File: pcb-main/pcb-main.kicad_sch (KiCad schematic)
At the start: 37 parts, among them J1 AVR-ISP-6, J2 Conn_02x06_Counter_Clockwise, M1 Stepper_Motor, SW1 SW_MEC_5E, SW2 SW_MEC_5E, U1 ATmega328P-AU, U2 HT1621B-LQFP-A, U3 VIM878, U4 PCF8563T, Y1 16MHz, Y2 32kHz

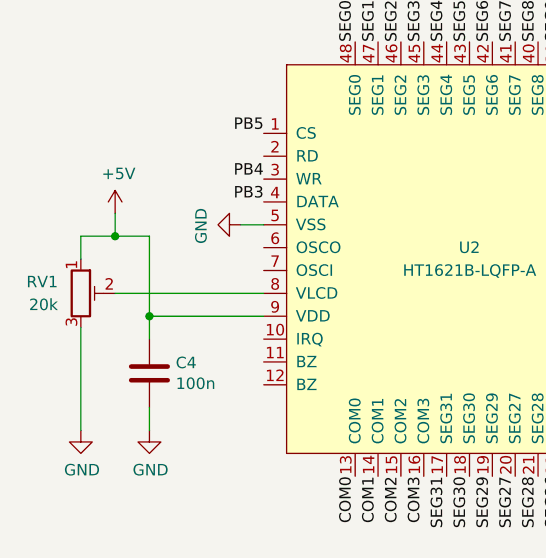
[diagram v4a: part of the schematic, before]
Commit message: changed pot
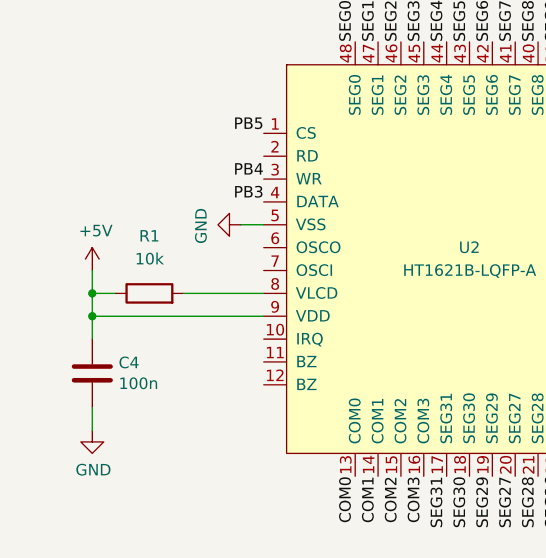
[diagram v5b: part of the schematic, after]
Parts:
- removed RV1: 20k, Potentiometer_SMD:Potentiometer_Bourns_TC33X_Vertical, symbol Device:R_Potentiometer_Trim
- added R1: 10k, Resistor_SMD:R_1206_3216Metric_Pad1.30x1.75mm_HandSolder, symbol Device:R
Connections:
- net +5V: now also R1.1
- net at U2.8 (VLCD): now also R1.2
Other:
- moved on the sheet: C4
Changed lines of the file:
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@@
   (junction (at 217.17 45.72) (diameter 0) (color 0 0 0 0)
   )
+  (junction (at 27.94 161.29) (diameter 0) (color 0 0 0 0)
+  )
   (junction (at 262.89 24.13) (diameter 0) (color 0 0 0 0)
   )
-  (junction (at 34.29 163.83) (diameter 0) (color 0 0 0 0)
-  )
   (junction (at 273.05 36.83) (diameter 0) (color 0 0 0 0)
   )
   (junction (at 227.33 63.5) (diameter 0) (color 0 0 0 0)
   )
-  (junction (at 30.48 154.94) (diameter 0) (color 0 0 0 0)
-  )
   (junction (at 186.69 36.83) (diameter 0) (color 0 0 0 0)
   )
@@
   (junction (at 227.33 50.8) (diameter 0) (color 0 0 0 0)
   )
+  (junction (at 27.94 163.83) (diameter 0) (color 0 0 0 0)
+  )
   (junction (at 54.61 25.4) (diameter 0) (color 0 0 0 0)
   )
@@
     (stroke (width 0) (type default) (color 0 0 0 0))
   )
-  (wire (pts (xy 34.29 163.83) (xy 34.29 154.94))
+  (wire (pts (xy 27.94 161.29) (xy 27.94 163.83))
     (stroke (width 0) (type default) (color 0 0 0 0))
   )
@@
     (stroke (width 0) (type default) (color 0 0 0 0))
   )
-  (wire (pts (xy 34.29 176.53) (xy 34.29 173.99))
+  (wire (pts (xy 27.94 176.53) (xy 27.94 173.99))
     (stroke (width 0) (type default) (color 0 0 0 0))
   )
@@
     (stroke (width 0) (type default) (color 0 0 0 0))
   )
-  (wire (pts (xy 26.67 154.94) (xy 26.67 157.48))
-    (stroke (width 0) (type default) (color 0 0 0 0))
-  )
   (wire (pts (xy 227.33 50.8) (xy 227.33 53.34))
     (stroke (width 0) (type default) (color 0 0 0 0))
@@
     (stroke (width 0) (type default) (color 0 0 0 0))
   )
-  (wire (pts (xy 34.29 154.94) (xy 30.48 154.94))
-    (stroke (width 0) (type default) (color 0 0 0 0))
-  )
   (wire (pts (xy 195.58 135.89) (xy 207.01 135.89))
     (stroke (width 0) (type default) (color 0 0 0 0))
@@
     (stroke (width 0) (type default) (color 0 0 0 0))
   )
-  (wire (pts (xy 30.48 152.4) (xy 30.48 154.94))
-    (stroke (width 0) (type default) (color 0 0 0 0))
-  )
-  (wire (pts (xy 26.67 165.1) (xy 26.67 176.53))
-    (stroke (width 0) (type default) (color 0 0 0 0))
-  )
   (wire (pts (xy 201.93 39.37) (xy 201.93 36.83))
     (stroke (width 0) (type default) (color 0 0 0 0))
@@
     (stroke (width 0) (type default) (color 0 0 0 0))
   )
+  (wire (pts (xy 30.48 161.29) (xy 27.94 161.29))
+    (stroke (width 0) (type default) (color 0 0 0 0))
+  )
   (wire (pts (xy 273.05 26.67) (xy 273.05 24.13))
     (stroke (width 0) (type default) (color 0 0 0 0))
@@
     (stroke (width 0) (type default) (color 0 0 0 0))
   )
-  (wire (pts (xy 30.48 154.94) (xy 26.67 154.94))
+  (wire (pts (xy 27.94 163.83) (xy 27.94 166.37))
     (stroke (width 0) (type default) (color 0 0 0 0))
   )
@@
     (stroke (width 0) (type default) (color 0 0 0 0))
   )
-  (wire (pts (xy 34.29 163.83) (xy 34.29 166.37))
+  (wire (pts (xy 27.94 163.83) (xy 46.99 163.83))
     (stroke (width 0) (type default) (color 0 0 0 0))
   )
@@
     (stroke (width 0) (type default) (color 0 0 0 0))
   )
+  (wire (pts (xy 38.1 161.29) (xy 46.99 161.29))
+    (stroke (width 0) (type default) (color 0 0 0 0))
+  )
   (wire (pts (xy 199.39 39.37) (xy 201.93 39.37))
     (stroke (width 0) (type default) (color 0 0 0 0))
@@
     (stroke (width 0) (type default) (color 0 0 0 0))
   )
-  (wire (pts (xy 30.48 161.29) (xy 46.99 161.29))
+  (wire (pts (xy 27.94 158.75) (xy 27.94 161.29))
     (stroke (width 0) (type default) (color 0 0 0 0))
   )
@@
   )
   (wire (pts (xy 118.11 90.17) (xy 118.11 92.71))
-    (stroke (width 0) (type default) (color 0 0 0 0))
-  )
-  (wire (pts (xy 34.29 163.83) (xy 46.99 163.83))
     (stroke (width 0) (type default) (color 0 0 0 0))
   )
@@
     (pin "1")
   )
-  (symbol (lib_id "power:+5V") (at 30.48 152.4 0) (unit 1)
-    (in_bom yes) (on_board yes)
-    (property "Reference" "#PWR0109" (id 0) (at 30.48 156.21 0)
-      (effects (font (size 1.27 1.27)) hide)
-    )
-    (property "Value" "+5V" (id 1) (at 30.861 148.0058 0))
-    (property "Footprint" "" (id 2) (at 30.48 152.4 0)
-      (effects (font (size 1.27 1.27)) hide)
-    )
-    (property "Datasheet" "" (id 3) (at 30.48 152.4 0)
+  (symbol (lib_id "power:+5V") (at 27.94 158.75 0) (unit 1)
+    (in_bom yes) (on_board yes)
+    (property "Reference" "#PWR0109" (id 0) (at 27.94 162.56 0)
+      (effects (font (size 1.27 1.27)) hide)
+    )
+    (property "Value" "+5V" (id 1) (at 28.321 154.3558 0))
+    (property "Footprint" "" (id 2) (at 27.94 158.75 0)
+      (effects (font (size 1.27 1.27)) hide)
+    )
+    (property "Datasheet" "" (id 3) (at 27.94 158.75 0)
       (effects (font (size 1.27 1.27)) hide)
     )
@@
     (pin "1")
   )
-  (symbol (lib_id "Device:C") (at 34.29 170.18 0) (unit 1)
-    (in_bom yes) (on_board yes)
-    (property "Reference" "C4" (id 0) (at 37.211 169.0116 0)
-      (effects (font (size 1.27 1.27)) (justify left))
-    )
-    (property "Value" "100n" (id 1) (at 37.211 171.323 0)
-      (effects (font (size 1.27 1.27)) (justify left))
-    )
-    (property "Footprint" "Capacitor_SMD:C_1206_3216Metric_Pad1.33x1.80mm_HandSolder" (id 2) (at 35.2552 173.99 0)
-      (effects (font (size 1.27 1.27)) hide)
-    )
-    (property "Datasheet" "~" (id 3) (at 34.29 170.18 0)
-      (effects (font (size 1.27 1.27)) hide)
-    )
-    (property "LCSC" "" (id 4) (at 34.29 170.18 0)
-      (effects (font (size 1.27 1.27)) hide)
-    )
-    (pin "1")
-    (pin "2")
-  )
-  (symbol (lib_id "power:GND") (at 26.67 176.53 0) (unit 1)
-    (in_bom yes) (on_board yes)
-    (property "Reference" "#PWR0107" (id 0) (at 26.67 182.88 0)
-      (effects (font (size 1.27 1.27)) hide)
-    )
-    (property "Value" "GND" (id 1) (at 26.797 180.9242 0))
-    (property "Footprint" "" (id 2) (at 26.67 176.53 0)
-      (effects (font (size 1.27 1.27)) hide)
-    )
-    (property "Datasheet" "" (id 3) (at 26.67 176.53 0)
-      (effects (font (size 1.27 1.27)) hide)
-    )
-    (pin "1")
+  (symbol (lib_id "Device:C") (at 27.94 170.18 0) (unit 1)
+    (in_bom yes) (on_board yes)
+    (property "Reference" "C4" (id 0) (at 30.861 169.0116 0)
+      (effects (font (size 1.27 1.27)) (justify left))
+    )
+    (property "Value" "100n" (id 1) (at 30.861 171.323 0)
+      (effects (font (size 1.27 1.27)) (justify left))
+    )
+    (property "Footprint" "Capacitor_SMD:C_1206_3216Metric_Pad1.33x1.80mm_HandSolder" (id 2) (at 28.9052 173.99 0)
+      (effects (font (size 1.27 1.27)) hide)
+    )
+    (property "Datasheet" "~" (id 3) (at 27.94 170.18 0)
+      (effects (font (size 1.27 1.27)) hide)
+    )
+    (property "LCSC" "" (id 4) (at 27.94 170.18 0)
+      (effects (font (size 1.27 1.27)) hide)
+    )
+    (pin "1")
+    (pin "2")
   )
   (symbol (lib_id "LED:WS2812B") (at 191.77 91.44 0) (unit 1)
@@
     (pin "1")
   )
-  (symbol (lib_id "Device:R_Potentiometer_Trim") (at 26.67 161.29 0) (unit 1)
+  (symbol (lib_id "Device:R") (at 34.29 161.29 90) (unit 1)
     (in_bom yes) (on_board yes) (fields_autoplaced)
-    (property "Reference" "RV1" (id 0) (at 24.13 160.0199 0)
-      (effects (font (size 1.27 1.27)) (justify right))
-    )
-    (property "Value" "20k" (id 1) (at 24.13 162.5599 0)
-      (effects (font (size 1.27 1.27)) (justify right))
-    )
-    (property "Footprint" "Potentiometer_SMD:Potentiometer_Bourns_TC33X_Vertical" (id 2) (at 26.67 161.29 0)
-      (effects (font (size 1.27 1.27)) hide)
-    )
-    (property "Datasheet" "~" (id 3) (at 26.67 161.29 0)
-      (effects (font (size 1.27 1.27)) hide)
-    )
-    (pin "1")
-    (pin "2")
-    (pin "3")
-  )
-  (symbol (lib_id "power:GND") (at 34.29 176.53 0) (unit 1)
-    (in_bom yes) (on_board yes)
-    (property "Reference" "#PWR0135" (id 0) (at 34.29 182.88 0)
-      (effects (font (size 1.27 1.27)) hide)
-    )
-    (property "Value" "GND" (id 1) (at 34.417 180.9242 0))
-    (property "Footprint" "" (id 2) (at 34.29 176.53 0)
-      (effects (font (size 1.27 1.27)) hide)
-    )
-    (property "Datasheet" "" (id 3) (at 34.29 176.53 0)
+    (property "Reference" "R1" (id 0) (at 34.29 154.94 90))
+    (property "Value" "10k" (id 1) (at 34.29 157.48 90))
+    (property "Footprint" "Resistor_SMD:R_1206_3216Metric_Pad1.30x1.75mm_HandSolder" (id 2) (at 34.29 163.068 90)
+      (effects (font (size 1.27 1.27)) hide)
+    )
+    (property "Datasheet" "~" (id 3) (at 34.29 161.29 0)
+      (effects (font (size 1.27 1.27)) hide)
+    )
+    (pin "1")
+    (pin "2")
+  )
+  (symbol (lib_id "power:GND") (at 27.94 176.53 0) (unit 1)
+    (in_bom yes) (on_board yes)
+    (property "Reference" "#PWR0135" (id 0) (at 27.94 182.88 0)
+      (effects (font (size 1.27 1.27)) hide)
+    )
+    (property "Value" "GND" (id 1) (at 28.067 180.9242 0))
+    (property "Footprint" "" (id 2) (at 27.94 176.53 0)
+      (effects (font (size 1.27 1.27)) hide)
+    )
+    (property "Datasheet" "" (id 3) (at 27.94 176.53 0)
       (effects (font (size 1.27 1.27)) hide)
     )
@@
       (reference "#PWR0106") (unit 1) (value "GND") (footprint "")
     )
-    (path "/00000000-0000-0000-0000-000061685286"
-      (reference "#PWR0107") (unit 1) (value "GND") (footprint "")
-    )
     (path "/00000000-0000-0000-0000-0000612e9872"
       (reference "#PWR0108") (unit 1) (value "GND") (footprint "")
@@
       (reference "M1") (unit 1) (value "Stepper_Motor") (footprint "footprints:Stepper Motor")
     )
+    (path "/48a77ebe-3e04-4302-a406-53d7b17c46cd"
+      (reference "R1") (unit 1) (value "10k") (footprint "Resistor_SMD:R_1206_3216Metric_Pad1.30x1.75mm_HandSolder")
+    )
     (path "/00000000-0000-0000-0000-000061a7ca87"
       (reference "R2") (unit 1) (value "10k") (footprint "Resistor_SMD:R_1206_3216Metric_Pad1.30x1.75mm_HandSolder")
@@
       (reference "R7") (unit 1) (value "10k") (footprint "Resistor_SMD:R_1206_3216Metric_Pad1.30x1.75mm_HandSolder")
     )
-    (path "/56197513-6506-4a24-beee-dd8ea3402d50"
-      (reference "RV1") (unit 1) (value "20k") (footprint "Potentiometer_SMD:Potentiometer_Bourns_TC33X_Vertical")
-    )
     (path "/00000000-0000-0000-0000-000061bb50e2"

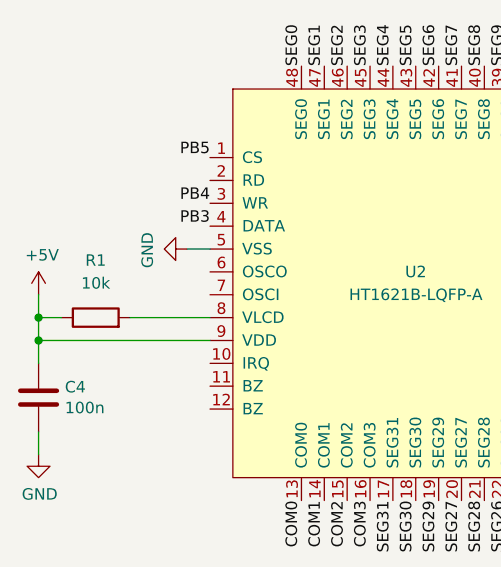
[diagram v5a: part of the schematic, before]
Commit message: changed lcd resistor to 100k
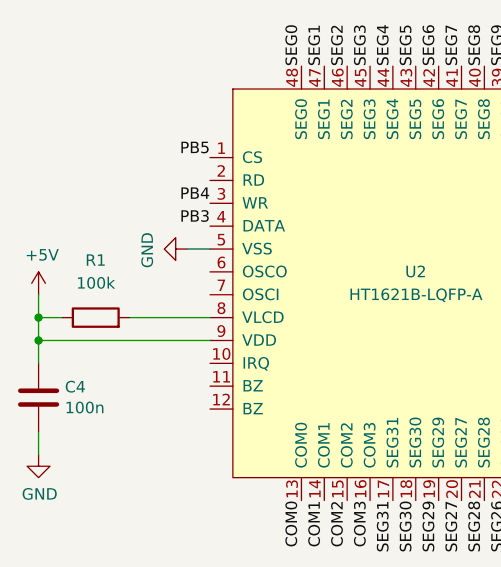
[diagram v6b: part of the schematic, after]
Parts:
- R1: value 10k -> 100k
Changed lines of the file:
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@@
     (in_bom yes) (on_board yes) (fields_autoplaced)
     (property "Reference" "R1" (id 0) (at 34.29 154.94 90))
-    (property "Value" "10k" (id 1) (at 34.29 157.48 90))
+    (property "Value" "100k" (id 1) (at 34.29 157.48 90))
     (property "Footprint" "Resistor_SMD:R_1206_3216Metric_Pad1.30x1.75mm_HandSolder" (id 2) (at 34.29 163.068 90)
       (effects (font (size 1.27 1.27)) hide)
@@
     )
     (path "/48a77ebe-3e04-4302-a406-53d7b17c46cd"
-      (reference "R1") (unit 1) (value "10k") (footprint "Resistor_SMD:R_1206_3216Metric_Pad1.30x1.75mm_HandSolder")
+      (reference "R1") (unit 1) (value "100k") (footprint "Resistor_SMD:R_1206_3216Metric_Pad1.30x1.75mm_HandSolder")
     )
     (path "/00000000-0000-0000-0000-000061a7ca87"

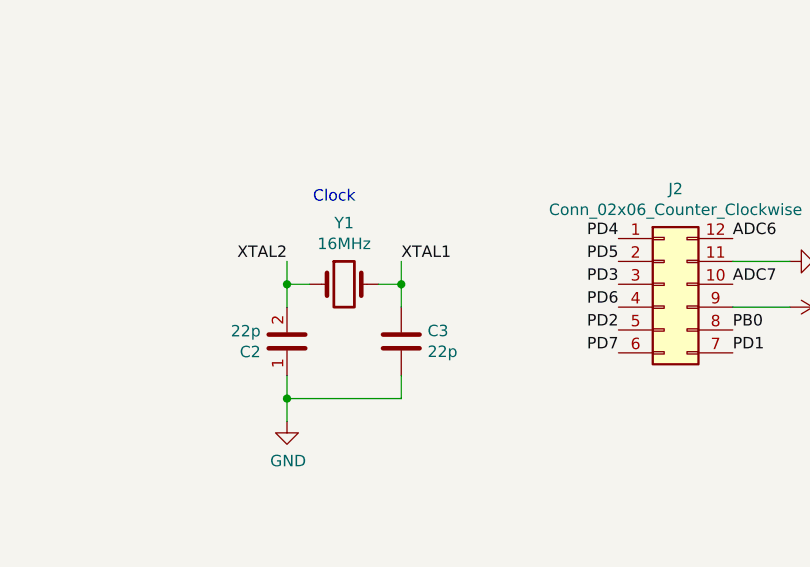
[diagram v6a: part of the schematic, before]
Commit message: resolves #52: crystal circuit
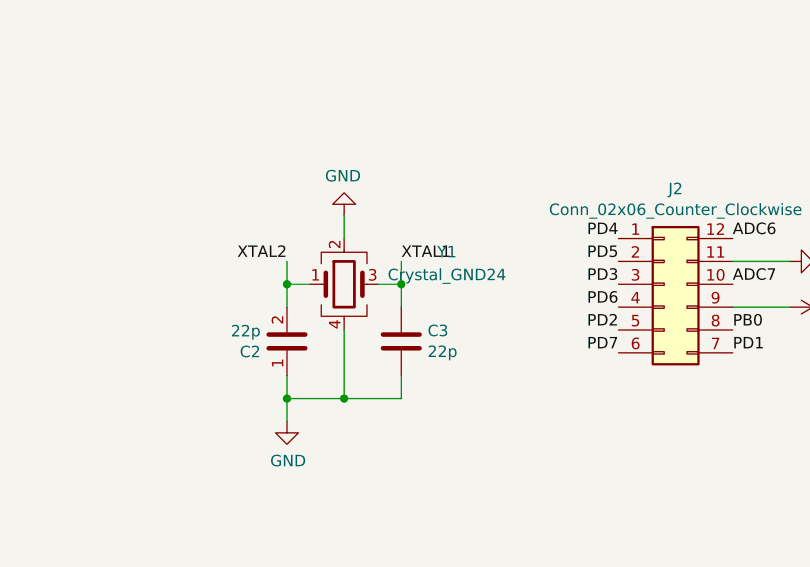
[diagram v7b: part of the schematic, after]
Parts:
- removed Y1: 16MHz, Crystal:Crystal_SMD_3225-4Pin_3.2x2.5mm, symbol Device:Crystal
- added Y1: Crystal_GND24, Crystal:Crystal_SMD_3225-4Pin_3.2x2.5mm, symbol Device:Crystal_GND24
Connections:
- net GND: now also Y1.2, Y1.4
- net XTAL1: now also Y1.3
- net XTAL2: now also Y1.1
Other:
- note removed: "Clock"
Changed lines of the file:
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@@
   (junction (at 201.93 39.37) (diameter 0) (color 0 0 0 0)
   )
+  (junction (at 111.76 102.87) (diameter 0) (color 0 0 0 0)
+  )
   (junction (at 34.29 25.4) (diameter 0) (color 0 0 0 0)
   )
@@
     (stroke (width 0) (type default) (color 0 0 0 0))
   )
+  (wire (pts (xy 111.76 102.87) (xy 105.41 102.87))
+    (stroke (width 0) (type default) (color 0 0 0 0))
+  )
   (wire (pts (xy 102.87 34.29) (xy 102.87 36.83))
     (stroke (width 0) (type default) (color 0 0 0 0))
@@
     (stroke (width 0) (type default) (color 0 0 0 0))
   )
+  (wire (pts (xy 111.76 82.55) (xy 111.76 85.09))
+    (stroke (width 0) (type default) (color 0 0 0 0))
+  )
   (wire (pts (xy 52.07 27.94) (xy 52.07 25.4))
     (stroke (width 0) (type default) (color 0 0 0 0))
@@
     (stroke (width 0) (type default) (color 0 0 0 0))
   )
+  (wire (pts (xy 111.76 95.25) (xy 111.76 102.87))
+    (stroke (width 0) (type default) (color 0 0 0 0))
+  )
   (wire (pts (xy 105.41 90.17) (xy 105.41 92.71))
     (stroke (width 0) (type default) (color 0 0 0 0))
@@
     (stroke (width 0) (type default) (color 0 0 0 0))
   )
-  (wire (pts (xy 118.11 102.87) (xy 105.41 102.87))
+  (wire (pts (xy 118.11 102.87) (xy 111.76 102.87))
     (stroke (width 0) (type default) (color 0 0 0 0))
   )
@@
   (text "ISP" (at 158.75 25.4 0)
     (effects (font (size 1.27 1.27)) (justify left bottom))
-  )
-  (text "Clock" (at 113.03 81.28 180)
-    (effects (font (size 1.27 1.27)) (justify right bottom))
   )
   (text "Mode button" (at 107.95 25.4 0)
@@
     (pin "2")
   )
-  (symbol (lib_id "Device:Crystal") (at 111.76 90.17 0) (unit 1)
-    (in_bom yes) (on_board yes)
-    (property "Reference" "Y1" (id 0) (at 111.76 83.3628 0))
-    (property "Value" "16MHz" (id 1) (at 111.76 85.6742 0))
-    (property "Footprint" "Crystal:Crystal_SMD_3225-4Pin_3.2x2.5mm" (id 2) (at 111.76 90.17 0)
-      (effects (font (size 1.27 1.27)) hide)
-    )
-    (property "Datasheet" "https://datasheet.lcsc.com/lcsc/2103291133_Yangxing-Tech-X322516MLB4SI_C13738.pdf" (id 3) (at 111.76 90.17 0)
-      (effects (font (size 1.27 1.27)) hide)
-    )
-    (pin "1")
-    (pin "2")
-  )
   (symbol (lib_name "C_1") (lib_id "Device:C") (at 105.41 96.52 180) (unit 1)
     (in_bom yes) (on_board yes)
@@
     (pin "1")
   )
+  (symbol (lib_id "power:GND") (at 111.76 82.55 180) (unit 1)
+    (in_bom yes) (on_board yes)
+    (property "Reference" "#PWR0107" (id 0) (at 111.76 76.2 0)
+      (effects (font (size 1.27 1.27)) hide)
+    )
+    (property "Value" "GND" (id 1) (at 111.633 78.1558 0))
+    (property "Footprint" "" (id 2) (at 111.76 82.55 0)
+      (effects (font (size 1.27 1.27)) hide)
+    )
+    (property "Datasheet" "" (id 3) (at 111.76 82.55 0)
+      (effects (font (size 1.27 1.27)) hide)
+    )
+    (pin "1")
+  )
   (symbol (lib_id "Device:R") (at 34.29 161.29 90) (unit 1)
     (in_bom yes) (on_board yes) (fields_autoplaced)
@@
     (pin "1")
   )
+  (symbol (lib_id "Device:Crystal_GND24") (at 111.76 90.17 0) (unit 1)
+    (in_bom yes) (on_board yes) (fields_autoplaced)
+    (property "Reference" "Y1" (id 0) (at 123.19 86.5886 0))
+    (property "Value" "Crystal_GND24" (id 1) (at 123.19 89.1286 0))
+    (property "Footprint" "Crystal:Crystal_SMD_3225-4Pin_3.2x2.5mm" (id 2) (at 111.76 90.17 0)
+      (effects (font (size 1.27 1.27)) hide)
+    )
+    (property "Datasheet" "~" (id 3) (at 111.76 90.17 0)
+      (effects (font (size 1.27 1.27)) hide)
+    )
+    (pin "1")
+    (pin "2")
+    (pin "3")
+    (pin "4")
+  )
   (symbol (lib_id "power:GND") (at 201.93 41.91 0) (unit 1)
     (in_bom yes) (on_board yes)
@@
       (reference "#PWR0106") (unit 1) (value "GND") (footprint "")
     )
+    (path "/179b8c95-887b-42fe-aa4e-c0f4b4e155a7"
+      (reference "#PWR0107") (unit 1) (value "GND") (footprint "")
+    )
     (path "/00000000-0000-0000-0000-0000612e9872"
       (reference "#PWR0108") (unit 1) (value "GND") (footprint "")
@@
       (reference "U4") (unit 1) (value "PCF8563T") (footprint "Package_SO:SOIC-8_3.9x4.9mm_P1.27mm")
     )
-    (path "/00000000-0000-0000-0000-00006149bb4a"
-      (reference "Y1") (unit 1) (value "16MHz") (footprint "Crystal:Crystal_SMD_3225-4Pin_3.2x2.5mm")
+    (path "/9ff564e8-8532-438a-84fa-bb0551b1f368"
+      (reference "Y1") (unit 1) (value "Crystal_GND24") (footprint "Crystal:Crystal_SMD_3225-4Pin_3.2x2.5mm")
     )
     (path "/00000000-0000-0000-0000-000061a72108"
